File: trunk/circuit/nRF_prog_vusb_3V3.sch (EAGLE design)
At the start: 26 parts, among them Q2 12MHz

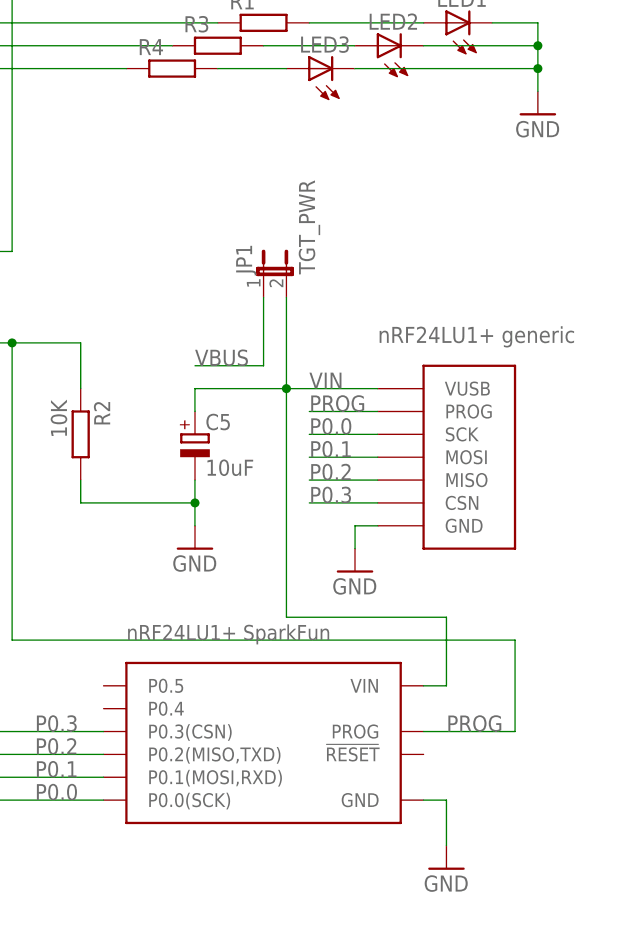
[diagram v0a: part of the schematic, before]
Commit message: 
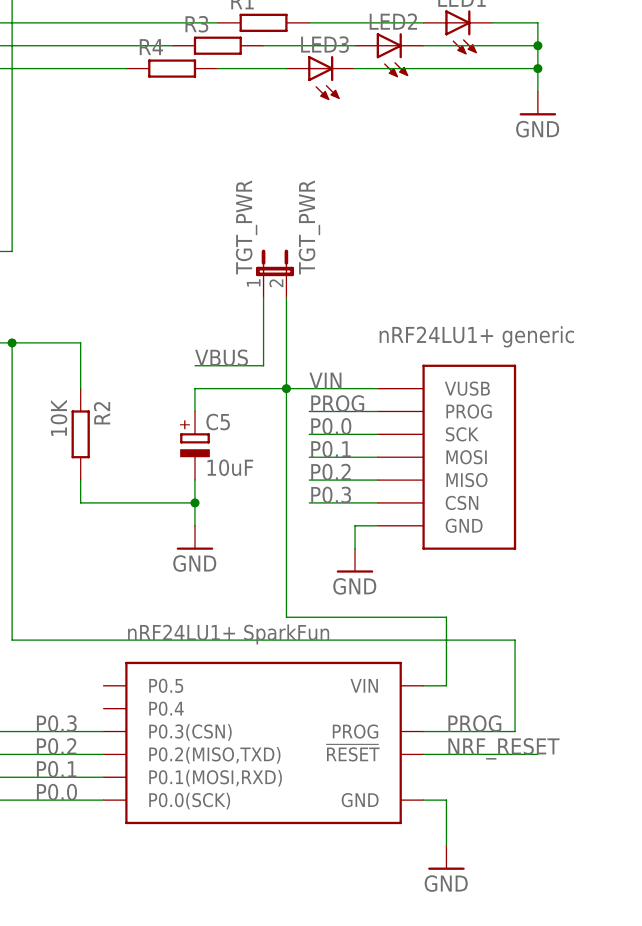
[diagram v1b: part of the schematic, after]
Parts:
- renumbered JP1 to TGT_PWR
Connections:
- new net NRF_RESET: U$2.!RESET!
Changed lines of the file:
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@@
 <part name="LED1" library="led" deviceset="LED" device="CHIPLED_0805"/>
 <part name="R1" library="rcl" deviceset="R-EU_" device="M0805"/>
-<part name="JP1" library="KileParts" deviceset="JP1E" device="" value="TGT_PWR"/>
+<part name="TGT_PWR" library="KileParts" deviceset="JP1E" device="" value="TGT_PWR"/>
 <part name="GND4" library="SparkFun" deviceset="GND" device=""/>
 <part name="C2" library="rcl" deviceset="C-EU" device="C0805K" value="470nF"/>
@@
 <instance part="LED1" gate="G$1" x="154.94" y="88.9" rot="R90"/>
 <instance part="R1" gate="G$1" x="134.62" y="88.9"/>
-<instance part="JP1" gate="A" x="134.62" y="60.96"/>
+<instance part="TGT_PWR" gate="A" x="134.62" y="60.96"/>
 <instance part="GND4" gate="1" x="144.78" y="27.94"/>
 <instance part="C2" gate="G$1" x="-12.7" y="86.36"/>
@@
 <segment>
 <pinref part="NRF_GEN" gate="G$1" pin="VUSB"/>
-<pinref part="JP1" gate="A" pin="2"/>
+<pinref part="TGT_PWR" gate="A" pin="2"/>
 <wire x1="147.32" y1="48.26" x2="137.16" y2="48.26" width="0.1524" layer="91"/>
 <wire x1="137.16" y1="48.26" x2="137.16" y2="58.42" width="0.1524" layer="91"/>
@@
 </segment>
 <segment>
-<pinref part="JP1" gate="A" pin="1"/>
+<pinref part="TGT_PWR" gate="A" pin="1"/>
 <wire x1="134.62" y1="58.42" x2="134.62" y2="50.8" width="0.1524" layer="91"/>
 <wire x1="134.62" y1="50.8" x2="127" y2="50.8" width="0.1524" layer="91"/>
@@
 </segment>
 </net>
+<net name="NRF_RESET" class="0">
+<segment>
+<pinref part="U$2" gate="G$1" pin="!RESET!"/>
+<wire x1="152.4" y1="7.62" x2="165.1" y2="7.62" width="0.1524" layer="91"/>
+<label x="154.94" y="7.62" size="1.778" layer="95"/>
+</segment>
+</net>

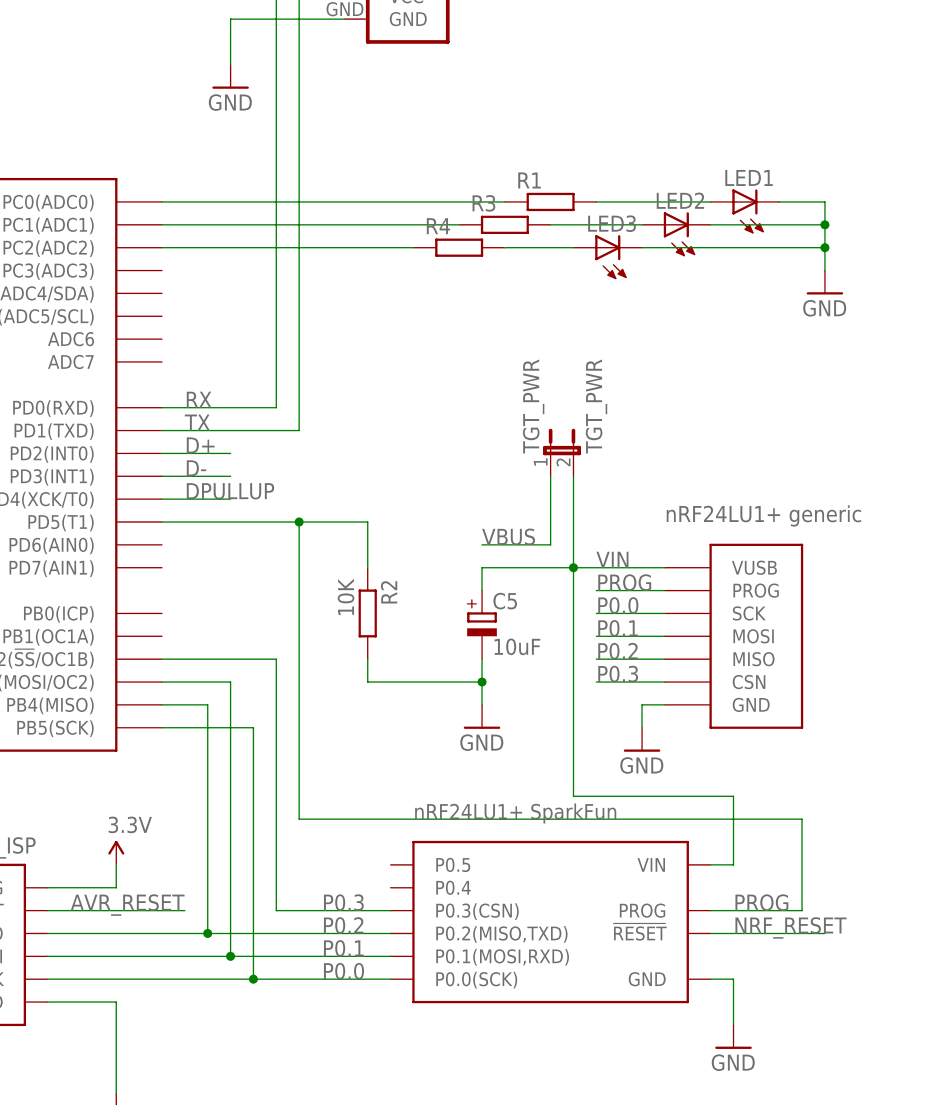
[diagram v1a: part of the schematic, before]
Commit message: New version works uses reset which hopefully fixes the problems with programming nRF24LU1+ It looks like it is necessary to reset the target before and/or after programming.
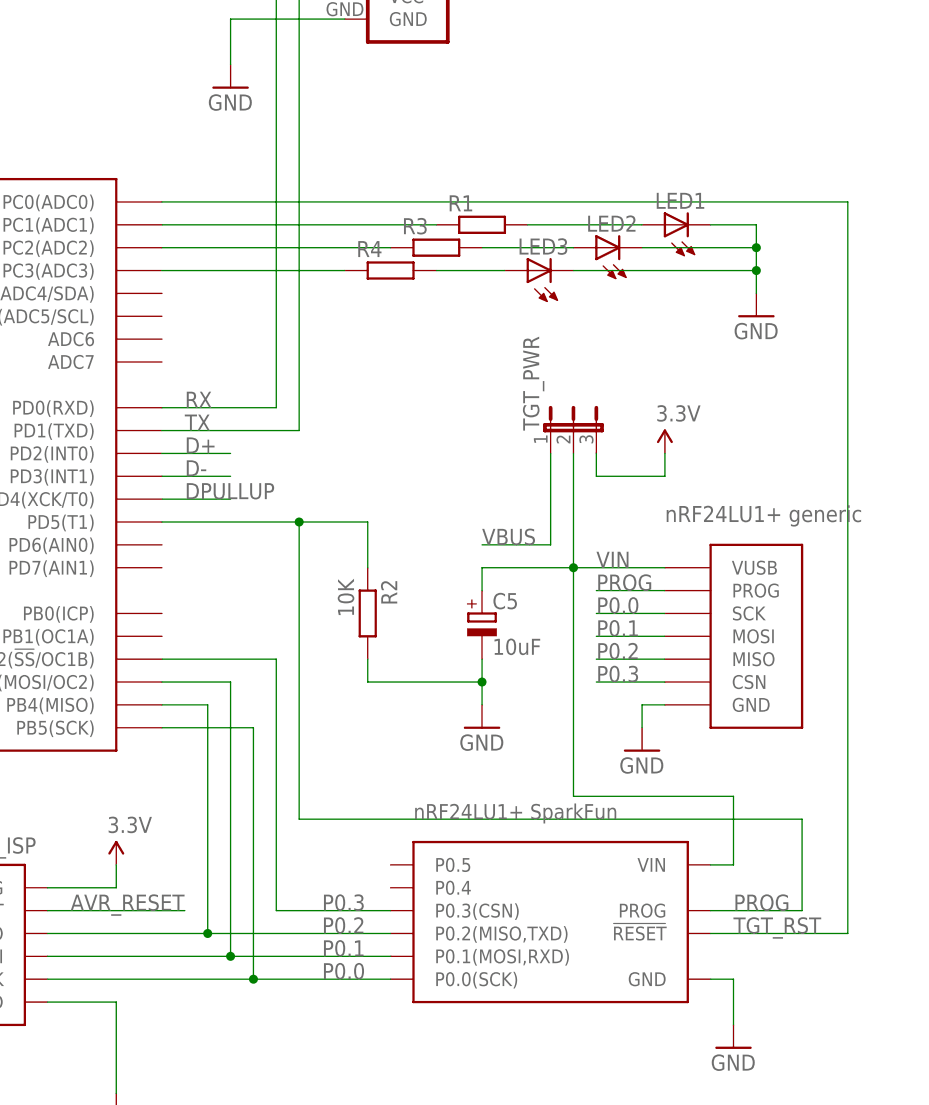
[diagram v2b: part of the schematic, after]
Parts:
- TGT_PWR: value TGT_PWR -> (none); device KileParts:JP1E -> jumper:JP2E
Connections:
- removed net N$17: R4.1, THE_BEAST.PC2(ADC2)
- removed net NRF_RESET: U$2.!RESET!
- new net N$13: R1.1, THE_BEAST.PC1(ADC1)
- new net TGT_RST: THE_BEAST.PC0(ADC0), U$2.!RESET!
- net 3.3V: now also TGT_PWR.3
- net N$8: now also R4.1, THE_BEAST.PC3(ADC3); no longer R1.1, THE_BEAST.PC0(ADC0)
- net N$9: now also THE_BEAST.PC2(ADC2); no longer THE_BEAST.PC1(ADC1)
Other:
- moved on the sheet: LED1, LED2, LED3, R1, R3, R4
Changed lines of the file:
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@@
 <part name="LED1" library="led" deviceset="LED" device="CHIPLED_0805"/>
 <part name="R1" library="rcl" deviceset="R-EU_" device="M0805"/>
-<part name="TGT_PWR" library="KileParts" deviceset="JP1E" device="" value="TGT_PWR"/>
 <part name="GND4" library="SparkFun" deviceset="GND" device=""/>
 <part name="C2" library="rcl" deviceset="C-EU" device="C0805K" value="470nF"/>
@@
 <part name="GND11" library="SparkFun" deviceset="GND" device=""/>
 <part name="P+5" library="SparkFun" deviceset="3.3V" device=""/>
+<part name="TGT_PWR" library="jumper" deviceset="JP2E" device=""/>
+<part name="P+4" library="SparkFun" deviceset="3.3V" device=""/>
 </parts>
 <sheets>
@@
 <instance part="GND2" gate="1" x="-2.54" y="68.58"/>
 <instance part="C1" gate="G$1" x="10.16" y="86.36"/>
-<instance part="LED1" gate="G$1" x="154.94" y="88.9" rot="R90"/>
-<instance part="R1" gate="G$1" x="134.62" y="88.9"/>
-<instance part="TGT_PWR" gate="A" x="134.62" y="60.96"/>
+<instance part="LED1" gate="G$1" x="147.32" y="86.36" rot="R90"/>
+<instance part="R1" gate="G$1" x="127" y="86.36"/>
 <instance part="GND4" gate="1" x="144.78" y="27.94"/>
 <instance part="C2" gate="G$1" x="-12.7" y="86.36"/>
 <instance part="R2" gate="G$1" x="114.3" y="43.18" rot="R270"/>
-<instance part="LED2" gate="G$1" x="147.32" y="86.36" rot="R90"/>
-<instance part="R3" gate="G$1" x="129.54" y="86.36"/>
-<instance part="LED3" gate="G$1" x="139.7" y="83.82" rot="R90"/>
-<instance part="R4" gate="G$1" x="124.46" y="83.82"/>
+<instance part="LED2" gate="G$1" x="139.7" y="83.82" rot="R90"/>
+<instance part="R3" gate="G$1" x="121.92" y="83.82"/>
+<instance part="LED3" gate="G$1" x="132.08" y="81.28" rot="R90"/>
+<instance part="R4" gate="G$1" x="116.84" y="81.28"/>
 <instance part="THE_BEAST" gate="G$1" x="66.04" y="63.5"/>
 <instance part="GND5" gate="1" x="20.32" y="50.8"/>
@@
 <instance part="C6" gate="G$1" x="25.4" y="63.5" rot="R90"/>
 <instance part="C3" gate="G$1" x="25.4" y="58.42" rot="R90"/>
-<instance part="GND3" gate="1" x="165.1" y="78.74"/>
+<instance part="GND3" gate="1" x="157.48" y="76.2"/>
 <instance part="GND11" gate="1" x="127" y="30.48"/>
 <instance part="P+5" gate="G$1" x="86.36" y="15.24"/>
+<instance part="TGT_PWR" gate="1" x="137.16" y="63.5"/>
+<instance part="P+4" gate="G$1" x="147.32" y="60.96"/>
 </instances>
 <busses>
@@
 <wire x1="86.36" y1="12.7" x2="86.36" y2="15.24" width="0.1524" layer="91"/>
 </segment>
+<segment>
+<pinref part="P+4" gate="G$1" pin="3.3V"/>
+<wire x1="147.32" y1="60.96" x2="147.32" y2="58.42" width="0.1524" layer="91"/>
+<pinref part="TGT_PWR" gate="1" pin="3"/>
+<wire x1="147.32" y1="58.42" x2="139.7" y2="58.42" width="0.1524" layer="91"/>
+<wire x1="139.7" y1="58.42" x2="139.7" y2="60.96" width="0.1524" layer="91"/>
+</segment>
 </net>
 <net name="GND" class="0">
@@
 </segment>
 <segment>
-<wire x1="165.1" y1="86.36" x2="165.1" y2="88.9" width="0.1524" layer="91"/>
+<wire x1="157.48" y1="83.82" x2="157.48" y2="86.36" width="0.1524" layer="91"/>
 <pinref part="LED2" gate="G$1" pin="C"/>
-<wire x1="152.4" y1="86.36" x2="165.1" y2="86.36" width="0.1524" layer="91"/>
+<wire x1="144.78" y1="83.82" x2="157.48" y2="83.82" width="0.1524" layer="91"/>
 <pinref part="LED1" gate="G$1" pin="C"/>
-<wire x1="160.02" y1="88.9" x2="165.1" y2="88.9" width="0.1524" layer="91"/>
+<wire x1="152.4" y1="86.36" x2="157.48" y2="86.36" width="0.1524" layer="91"/>
 <pinref part="LED3" gate="G$1" pin="C"/>
-<wire x1="144.78" y1="83.82" x2="165.1" y2="83.82" width="0.1524" layer="91"/>
-<wire x1="165.1" y1="83.82" x2="165.1" y2="86.36" width="0.1524" layer="91"/>
-<junction x="165.1" y="86.36"/>
+<wire x1="137.16" y1="81.28" x2="157.48" y2="81.28" width="0.1524" layer="91"/>
+<wire x1="157.48" y1="81.28" x2="157.48" y2="83.82" width="0.1524" layer="91"/>
+<junction x="157.48" y="83.82"/>
 <pinref part="GND3" gate="1" pin="GND"/>
-<wire x1="165.1" y1="83.82" x2="165.1" y2="81.28" width="0.1524" layer="91"/>
-<junction x="165.1" y="83.82"/>
+<wire x1="157.48" y1="81.28" x2="157.48" y2="78.74" width="0.1524" layer="91"/>
+<junction x="157.48" y="81.28"/>
 </segment>
 <segment>
@@
 <segment>
 <pinref part="NRF_GEN" gate="G$1" pin="VUSB"/>
-<pinref part="TGT_PWR" gate="A" pin="2"/>
 <wire x1="147.32" y1="48.26" x2="137.16" y2="48.26" width="0.1524" layer="91"/>
-<wire x1="137.16" y1="48.26" x2="137.16" y2="58.42" width="0.1524" layer="91"/>
 <label x="139.7" y="48.26" size="1.778" layer="95"/>
 <pinref part="U$2" gate="G$1" pin="VIN"/>
@@
 <wire x1="137.16" y1="48.26" x2="127" y2="48.26" width="0.1524" layer="91"/>
 <wire x1="127" y1="48.26" x2="127" y2="45.72" width="0.1524" layer="91"/>
+<pinref part="TGT_PWR" gate="1" pin="2"/>
+<wire x1="137.16" y1="60.96" x2="137.16" y2="48.26" width="0.1524" layer="91"/>
 </segment>
 </net>
@@
 </segment>
 </net>
-<net name="N$8" class="0">
-<segment>
-<pinref part="THE_BEAST" gate="G$1" pin="PC0(ADC0)"/>
-<pinref part="R1" gate="G$1" pin="1"/>
-<wire x1="91.44" y1="88.9" x2="129.54" y2="88.9" width="0.1524" layer="91"/>
-</segment>
-</net>
-<net name="N$9" class="0">
-<segment>
-<pinref part="R3" gate="G$1" pin="1"/>
-<pinref part="THE_BEAST" gate="G$1" pin="PC1(ADC1)"/>
-<wire x1="124.46" y1="86.36" x2="91.44" y2="86.36" width="0.1524" layer="91"/>
-</segment>
-</net>
-<net name="N$17" class="0">
-<segment>
-<pinref part="THE_BEAST" gate="G$1" pin="PC2(ADC2)"/>
-<pinref part="R4" gate="G$1" pin="1"/>
-<wire x1="91.44" y1="83.82" x2="119.38" y2="83.82" width="0.1524" layer="91"/>
-</segment>
-</net>
 <net name="N$18" class="0">
 <segment>
 <pinref part="R4" gate="G$1" pin="2"/>
 <pinref part="LED3" gate="G$1" pin="A"/>
-<wire x1="129.54" y1="83.82" x2="137.16" y2="83.82" width="0.1524" layer="91"/>
+<wire x1="121.92" y1="81.28" x2="129.54" y2="81.28" width="0.1524" layer="91"/>
 </segment>
 </net>
@@
 <pinref part="R3" gate="G$1" pin="2"/>
 <pinref part="LED2" gate="G$1" pin="A"/>
-<wire x1="134.62" y1="86.36" x2="144.78" y2="86.36" width="0.1524" layer="91"/>
+<wire x1="127" y1="83.82" x2="137.16" y2="83.82" width="0.1524" layer="91"/>
 </segment>
 </net>
@@
 <pinref part="R1" gate="G$1" pin="2"/>
 <pinref part="LED1" gate="G$1" pin="A"/>
-<wire x1="139.7" y1="88.9" x2="152.4" y2="88.9" width="0.1524" layer="91"/>
+<wire x1="132.08" y1="86.36" x2="144.78" y2="86.36" width="0.1524" layer="91"/>
 </segment>
 </net>
@@
 </segment>
 <segment>
-<pinref part="TGT_PWR" gate="A" pin="1"/>
-<wire x1="134.62" y1="58.42" x2="134.62" y2="50.8" width="0.1524" layer="91"/>
 <wire x1="134.62" y1="50.8" x2="127" y2="50.8" width="0.1524" layer="91"/>
 <label x="127" y="50.8" size="1.778" layer="95"/>
-</segment>
-</net>
-<net name="NRF_RESET" class="0">
+<pinref part="TGT_PWR" gate="1" pin="1"/>
+<wire x1="134.62" y1="50.8" x2="134.62" y2="60.96" width="0.1524" layer="91"/>
+</segment>
+</net>
+<net name="TGT_RST" class="0">
 <segment>
 <pinref part="U$2" gate="G$1" pin="!RESET!"/>
-<wire x1="152.4" y1="7.62" x2="165.1" y2="7.62" width="0.1524" layer="91"/>
+<wire x1="152.4" y1="7.62" x2="167.64" y2="7.62" width="0.1524" layer="91"/>
 <label x="154.94" y="7.62" size="1.778" layer="95"/>
-</segment>
-</net>
+<wire x1="167.64" y1="7.62" x2="167.64" y2="88.9" width="0.1524" layer="91"/>
+<pinref part="THE_BEAST" gate="G$1" pin="PC0(ADC0)"/>
+<wire x1="167.64" y1="88.9" x2="91.44" y2="88.9" width="0.1524" layer="91"/>
+</segment>
+</net>
+<net name="N$8" class="0">
+<segment>
+<pinref part="R4" gate="G$1" pin="1"/>
+<pinref part="THE_BEAST" gate="G$1" pin="PC3(ADC3)"/>
+<wire x1="111.76" y1="81.28" x2="91.44" y2="81.28" width="0.1524" layer="91"/>
+</segment>
+</net>
+<net name="N$9" class="0">
+<segment>
+<pinref part="R3" gate="G$1" pin="1"/>
+<pinref part="THE_BEAST" gate="G$1" pin="PC2(ADC2)"/>
+<wire x1="116.84" y1="83.82" x2="91.44" y2="83.82" width="0.1524" layer="91"/>
+</segment>
+</net>
+<net name="N$13" class="0">
+<segment>
+<pinref part="R1" gate="G$1" pin="1"/>
+<pinref part="THE_BEAST" gate="G$1" pin="PC1(ADC1)"/>
+<wire x1="121.92" y1="86.36" x2="91.44" y2="86.36" width="0.1524" layer="91"/>
+</segment>
+</net>
